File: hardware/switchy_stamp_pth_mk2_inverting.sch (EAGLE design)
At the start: 20 parts, among them IC1 MC34063

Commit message: fixed a few mistakes, still rearranging
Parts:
- C1: value 68uF -> 100uF
- H1, H2, H3, H4: value HOLE#4 -> HOLE#2; device A_butts:HOLE#4 -> A_butts:HOLE#2
- L1: device A_butts:INDUCTORRLB0912 -> A_butts:INDUCTORRADIAL-PTH-3-BY-6.7DIA
- ON/OFF: value SWITCH-SPDTPTH-RA-2.54MM -> SWITCH-SPDTPTH-VERT-2.54MM; device A_butts:SWITCH-SPDTPTH-RA-2.54MM -> A_butts:SWITCH-SPDTPTH-VERT-2.54MM
- R3: device A_butts:RESISTOR -> A_butts:RESISTORAXIAL-PTH-7.68MM
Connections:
- net N$6: now also L1.1
- net VOUT-: no longer L1.1
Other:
- moved on the sheet: C1, C2, C3, D1, D2, F1, IN, L1, LED1, ON/OFF, OUT, R4

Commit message: redo
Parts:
- R1, R2: device A_butts:RESISTORPTH-AXIAL-5.08MM -> A_butts:RESISTORAXIAL-PTH-7.68MM
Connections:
- net N$4: now also F1.1; no longer ON/OFF.COM
- net N$8: now also F1.2, ON/OFF.COM; no longer F1.1, ON/OFF.NC
- net VIN+: now also ON/OFF.NO; no longer F1.2
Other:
- moved on the sheet: F1, ON/OFF
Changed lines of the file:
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@@
 <?xml version="1.0" encoding="utf-8"?>
 <!DOCTYPE eagle SYSTEM "eagle.dtd">
-<eagle version="6.5.0">
+<eagle version="6.4">
 <drawing>
 <settings>
@@
 <setting verticaltext="up"/>
 </settings>
-<grid distance="100" unitdist="mil" unit="mil" style="lines" multiple="1" display="yes" altdistance="1" altunitdist="mil" altunit="mil"/>
+<grid distance="100" unitdist="mil" unit="mil" style="lines" multiple="1" display="yes" altdistance="1" altunitdist="mm" altunit="mm"/>
 <layers>
 <layer number="1" name="Top" color="4" fill="1" visible="yes" active="no"/>
@@
 <part name="F1" library="A_butts" deviceset="PTC" device="PTH"/>
 <part name="R3" library="A_butts" deviceset="RESISTOR" device="AXIAL-PTH-7.68MM" value="Iset"/>
-<part name="R1" library="A_butts" deviceset="RESISTOR" device="PTH-AXIAL-5.08MM" value="100R"/>
-<part name="R2" library="A_butts" deviceset="RESISTOR" device="PTH-AXIAL-5.08MM" value="300R"/>
+<part name="R1" library="A_butts" deviceset="RESISTOR" device="AXIAL-PTH-7.68MM" value="100R"/>
+<part name="R2" library="A_butts" deviceset="RESISTOR" device="AXIAL-PTH-7.68MM" value="300R"/>
 <part name="D2" library="A_butts" deviceset="DIODE-SCHOTTKY" device="DO-41" value="1N5819"/>
 <part name="D1" library="A_butts" deviceset="DIODE-SCHOTTKY" device="DO-41" value="1N5819"/>
@@
 <instance part="C2" gate="G$1" x="134.62" y="15.24"/>
 <instance part="C3" gate="G$1" x="104.14" y="33.02"/>
-<instance part="F1" gate="G$1" x="35.56" y="40.64" rot="R180"/>
+<instance part="F1" gate="G$1" x="48.26" y="25.4" rot="R180"/>
 <instance part="R3" gate="G$1" x="68.58" y="48.26"/>
 <instance part="R1" gate="G$1" x="73.66" y="15.24" rot="R90"/>
@@
 <instance part="H1" gate="G$1" x="119.38" y="66.04"/>
 <instance part="H3" gate="G$1" x="119.38" y="60.96"/>
-<instance part="ON/OFF" gate="G$1" x="40.64" y="20.32" rot="MR0"/>
+<instance part="ON/OFF" gate="G$1" x="35.56" y="43.18" rot="MR0"/>
 </instances>
 <busses>
@@
 <pinref part="IN" gate="G$1" pin="1"/>
 <wire x1="22.86" y1="40.64" x2="25.4" y2="40.64" width="0.1524" layer="91"/>
-<pinref part="F1" gate="G$1" pin="2"/>
-<wire x1="25.4" y1="40.64" x2="27.94" y2="40.64" width="0.1524" layer="91"/>
+<pinref part="ON/OFF" gate="G$1" pin="NO"/>
+<wire x1="25.4" y1="40.64" x2="30.48" y2="40.64" width="0.1524" layer="91"/>
 <junction x="25.4" y="40.64"/>
 </segment>
@@
 <net name="N$5" class="0">
 <segment>
-<pinref part="D1" gate="G$1" pin="C"/>
 <pinref part="R3" gate="G$1" pin="1"/>
 <wire x1="63.5" y1="48.26" x2="60.96" y2="48.26" width="0.1524" layer="91"/>
 <wire x1="60.96" y1="48.26" x2="60.96" y2="38.1" width="0.1524" layer="91"/>
-<wire x1="60.96" y1="38.1" x2="58.42" y2="38.1" width="0.1524" layer="91"/>
 <junction x="60.96" y="38.1"/>
 <pinref part="IC1" gate="G$1" pin="VCC"/>
@@
 <wire x1="60.96" y1="38.1" x2="60.96" y2="17.78" width="0.1524" layer="91"/>
 <junction x="60.96" y="38.1"/>
+<pinref part="D1" gate="G$1" pin="C"/>
+<wire x1="58.42" y1="38.1" x2="60.96" y2="38.1" width="0.1524" layer="91"/>
 </segment>
 </net>
@@
 </segment>
 </net>
-<net name="N$4" class="0">
-<segment>
-<pinref part="D1" gate="G$1" pin="A"/>
-<pinref part="ON/OFF" gate="G$1" pin="COM"/>
-<wire x1="45.72" y1="20.32" x2="50.8" y2="20.32" width="0.1524" layer="91"/>
-<wire x1="50.8" y1="20.32" x2="50.8" y2="38.1" width="0.1524" layer="91"/>
-<wire x1="50.8" y1="38.1" x2="53.34" y2="38.1" width="0.1524" layer="91"/>
-</segment>
-</net>
-<net name="N$8" class="0">
-<segment>
-<pinref part="F1" gate="G$1" pin="1"/>
-<pinref part="ON/OFF" gate="G$1" pin="NC"/>
-<wire x1="35.56" y1="22.86" x2="30.48" y2="22.86" width="0.1524" layer="91"/>
-<wire x1="30.48" y1="22.86" x2="30.48" y2="33.02" width="0.1524" layer="91"/>
-<wire x1="30.48" y1="33.02" x2="43.18" y2="33.02" width="0.1524" layer="91"/>
-<wire x1="43.18" y1="33.02" x2="43.18" y2="40.64" width="0.1524" layer="91"/>
-<wire x1="43.18" y1="40.64" x2="40.64" y2="40.64" width="0.1524" layer="91"/>
-</segment>
-</net>
 <net name="N$6" class="0">
 <segment>
@@
 </segment>
 </net>
+<net name="N$4" class="0">
+<segment>
+<pinref part="D1" gate="G$1" pin="A"/>
+<pinref part="F1" gate="G$1" pin="1"/>
+<wire x1="53.34" y1="25.4" x2="53.34" y2="38.1" width="0.1524" layer="91"/>
+</segment>
+</net>
+<net name="N$8" class="0">
+<segment>
+<pinref part="F1" gate="G$1" pin="2"/>
+<pinref part="ON/OFF" gate="G$1" pin="COM"/>
+<wire x1="40.64" y1="43.18" x2="40.64" y2="25.4" width="0.1524" layer="91"/>
+</segment>
+</net>

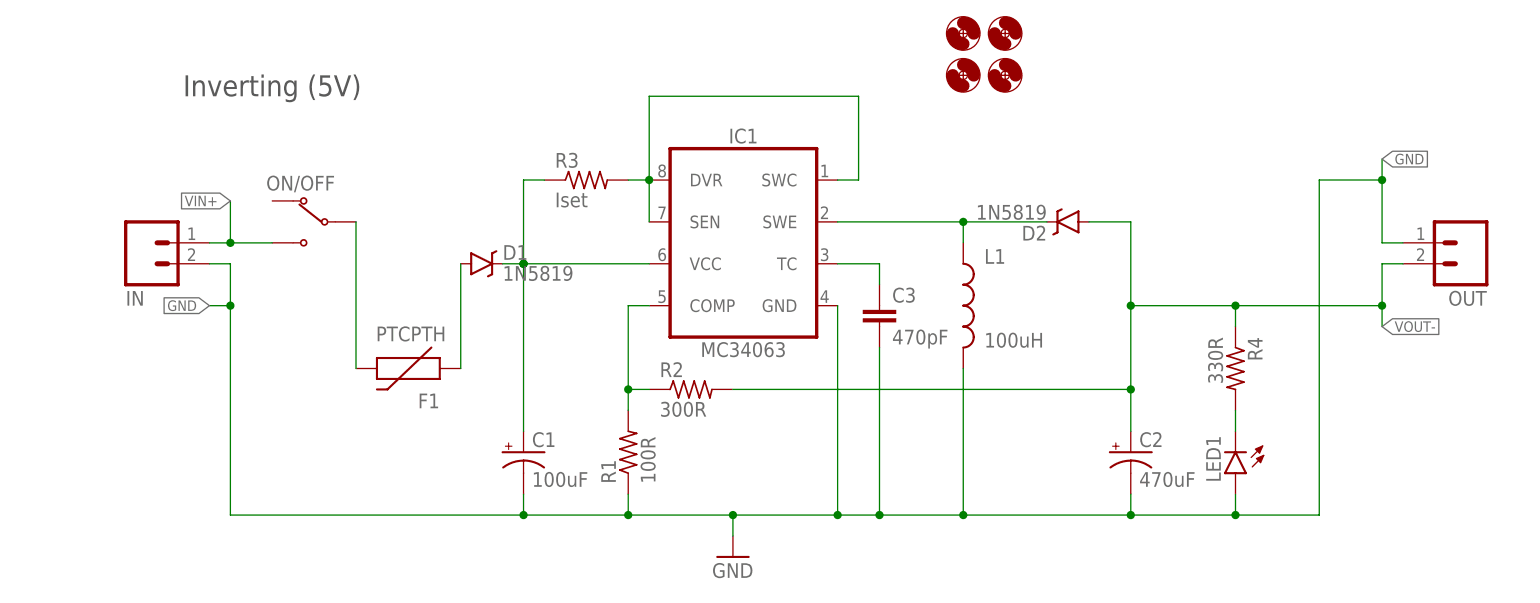
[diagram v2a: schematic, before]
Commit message: a saner layout with a few fixes, but still not complete
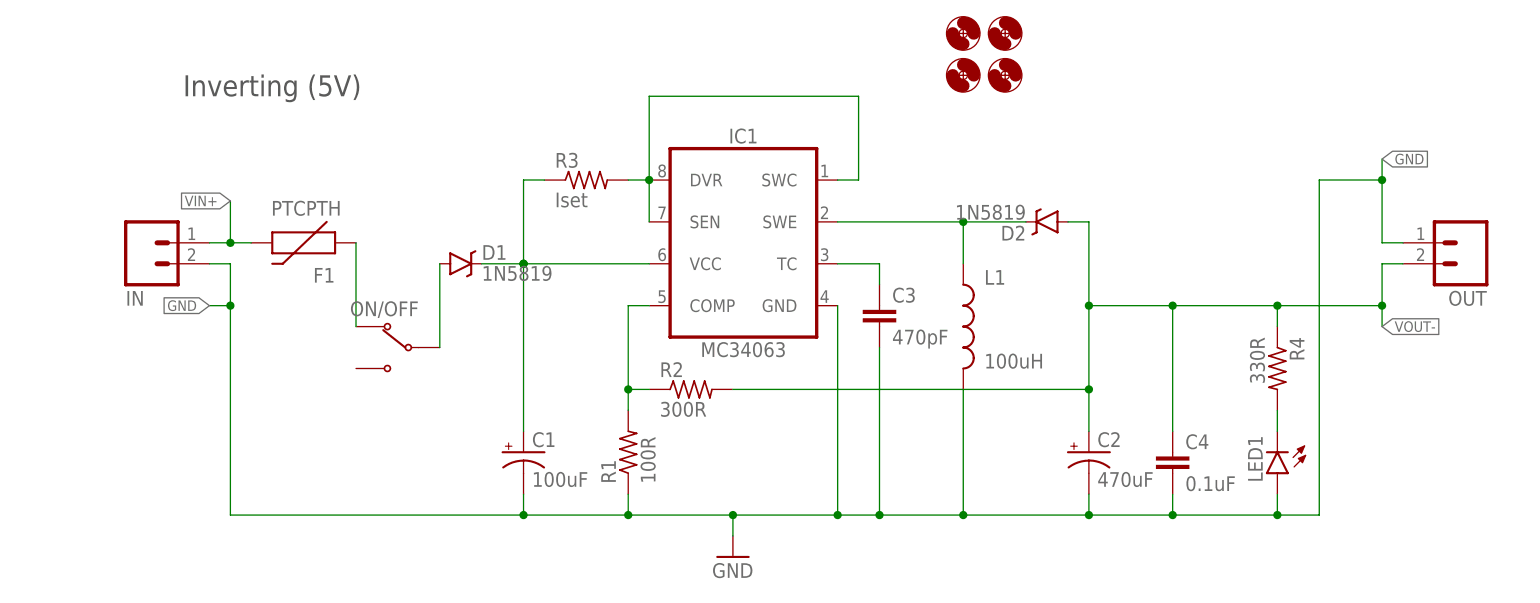
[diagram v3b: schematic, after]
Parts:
- added C4: 0.1uF, A_butts:CAPACITOR-CERAMIC025-024X044
- C1: device A_butts:CAPACITOR-POLARIZEDE2.5-6 -> A_butts:CAPACITOR-POLARIZEDE2.5-7
- ON/OFF: value SWITCH-SPDTPTH-VERT-2.54MM -> SWITCH-SPDTPTH-RA-2.54MM; device A_butts:SWITCH-SPDTPTH-VERT-2.54MM -> A_butts:SWITCH-SPDTPTH-RA-2.54MM
- R1, R2, R3: device A_butts:RESISTORAXIAL-PTH-7.68MM -> A_butts:RESISTORPTH-AXIAL-7.68MM
- R4: device A_butts:RESISTORPTH-AXIAL-5.08MM -> A_butts:RESISTORPTH-AXIAL-7.68MM
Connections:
- net GND: now also C4.2
- net N$4: now also ON/OFF.NC; no longer D1.A
- net N$8: now also D1.A; no longer F1.2
- net VIN+: now also F1.2; no longer ON/OFF.NO
- net VOUT-: now also C4.1
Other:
- moved on the sheet: C2, D1, D2, F1, L1, LED1, ON/OFF, R4

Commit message: blah
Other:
- moved on the sheet: L1
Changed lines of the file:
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@@
 <?xml version="1.0" encoding="utf-8"?>
 <!DOCTYPE eagle SYSTEM "eagle.dtd">
-<eagle version="6.5.0">
+<eagle version="6.4">
 <drawing>
 <settings>
@@
 <grid distance="100" unitdist="mil" unit="mil" style="lines" multiple="1" display="yes" altdistance="1" altunitdist="mil" altunit="mil"/>
 <layers>
-<layer number="1" name="Top" color="4" fill="1" visible="yes" active="no"/>
-<layer number="16" name="Bottom" color="1" fill="1" visible="yes" active="no"/>
-<layer number="17" name="Pads" color="2" fill="1" visible="yes" active="no"/>
-<layer number="18" name="Vias" color="2" fill="1" visible="yes" active="no"/>
-<layer number="19" name="Unrouted" color="6" fill="1" visible="yes" active="no"/>
-<layer number="20" name="Dimension" color="15" fill="1" visible="yes" active="no"/>
-<layer number="21" name="tPlace" color="7" fill="1" visible="yes" active="no"/>
-<layer number="22" name="bPlace" color="7" fill="1" visible="yes" active="no"/>
-<layer number="23" name="tOrigins" color="15" fill="1" visible="yes" active="no"/>
-<layer number="24" name="bOrigins" color="15" fill="1" visible="yes" active="no"/>
-<layer number="25" name="tNames" color="7" fill="1" visible="yes" active="no"/>
-<layer number="26" name="bNames" color="7" fill="1" visible="yes" active="no"/>
-<layer number="27" name="tValues" color="7" fill="1" visible="yes" active="no"/>
-<layer number="28" name="bValues" color="7" fill="1" visible="yes" active="no"/>
+<layer number="1" name="Top" color="4" fill="1" visible="no" active="no"/>
+<layer number="16" name="Bottom" color="1" fill="1" visible="no" active="no"/>
+<layer number="17" name="Pads" color="2" fill="1" visible="no" active="no"/>
+<layer number="18" name="Vias" color="2" fill="1" visible="no" active="no"/>
+<layer number="19" name="Unrouted" color="6" fill="1" visible="no" active="no"/>
+<layer number="20" name="Dimension" color="15" fill="1" visible="no" active="no"/>
+<layer number="21" name="tPlace" color="7" fill="1" visible="no" active="no"/>
+<layer number="22" name="bPlace" color="7" fill="1" visible="no" active="no"/>
+<layer number="23" name="tOrigins" color="15" fill="1" visible="no" active="no"/>
+<layer number="24" name="bOrigins" color="15" fill="1" visible="no" active="no"/>
+<layer number="25" name="tNames" color="7" fill="1" visible="no" active="no"/>
+<layer number="26" name="bNames" color="7" fill="1" visible="no" active="no"/>
+<layer number="27" name="tValues" color="7" fill="1" visible="no" active="no"/>
+<layer number="28" name="bValues" color="7" fill="1" visible="no" active="no"/>
 <layer number="29" name="tStop" color="7" fill="3" visible="no" active="no"/>
 <layer number="30" name="bStop" color="7" fill="6" visible="no" active="no"/>
@@
 <layer number="35" name="tGlue" color="7" fill="4" visible="no" active="no"/>
 <layer number="36" name="bGlue" color="7" fill="5" visible="no" active="no"/>
-<layer number="37" name="tTest" color="7" fill="1" visible="yes" active="no"/>
-<layer number="38" name="bTest" color="7" fill="1" visible="yes" active="no"/>
+<layer number="37" name="tTest" color="7" fill="1" visible="no" active="no"/>
+<layer number="38" name="bTest" color="7" fill="1" visible="no" active="no"/>
 <layer number="39" name="tKeepout" color="4" fill="11" visible="no" active="no"/>
 <layer number="40" name="bKeepout" color="1" fill="11" visible="no" active="no"/>
@@
 <layer number="44" name="Drills" color="7" fill="1" visible="no" active="no"/>
 <layer number="45" name="Holes" color="7" fill="1" visible="no" active="no"/>
-<layer number="46" name="Milling" color="3" fill="1" visible="yes" active="no"/>
-<layer number="47" name="Measures" color="7" fill="1" visible="yes" active="no"/>
-<layer number="48" name="Document" color="7" fill="1" visible="yes" active="no"/>
-<layer number="49" name="Reference" color="7" fill="1" visible="yes" active="no"/>
-<layer number="50" name="dxf" color="7" fill="1" visible="yes" active="no"/>
-<layer number="51" name="tDocu" color="7" fill="1" visible="yes" active="no"/>
-<layer number="52" name="bDocu" color="7" fill="1" visible="yes" active="no"/>
-<layer number="53" name="tGND_GNDA" color="7" fill="9" visible="yes" active="no"/>
-<layer number="54" name="bGND_GNDA" color="1" fill="9" visible="yes" active="no"/>
-<layer number="56" name="wert" color="7" fill="1" visible="yes" active="no"/>
-<layer number="57" name="tCAD" color="7" fill="1" visible="yes" active="no"/>
+<layer number="46" name="Milling" color="3" fill="1" visible="no" active="no"/>
+<layer number="47" name="Measures" color="7" fill="1" visible="no" active="no"/>
+<layer number="48" name="Document" color="7" fill="1" visible="no" active="no"/>
+<layer number="49" name="Reference" color="7" fill="1" visible="no" active="no"/>
+<layer number="50" name="dxf" color="7" fill="1" visible="no" active="no"/>
+<layer number="51" name="tDocu" color="7" fill="1" visible="no" active="no"/>
+<layer number="52" name="bDocu" color="7" fill="1" visible="no" active="no"/>
+<layer number="53" name="tGND_GNDA" color="7" fill="9" visible="no" active="no"/>
+<layer number="54" name="bGND_GNDA" color="1" fill="9" visible="no" active="no"/>
+<layer number="56" name="wert" color="7" fill="1" visible="no" active="no"/>
+<layer number="57" name="tCAD" color="7" fill="1" visible="no" active="no"/>
 <layer number="91" name="Nets" color="2" fill="1" visible="yes" active="yes"/>
 <layer number="92" name="Busses" color="1" fill="1" visible="yes" active="yes"/>
@@
 </plain>
 <instances>
-<instance part="L1" gate="G$1" x="114.3" y="30.48"/>
+<instance part="L1" gate="G$1" x="114.3" y="33.02"/>
 <instance part="C1" gate="G$1" x="60.96" y="15.24"/>
 <instance part="C2" gate="G$1" x="129.54" y="15.24"/>
@@
 <junction x="99.06" y="7.62"/>
 <pinref part="L1" gate="G$1" pin="2"/>
-<wire x1="114.3" y1="7.62" x2="114.3" y2="22.86" width="0.1524" layer="91"/>
+<wire x1="114.3" y1="7.62" x2="114.3" y2="25.4" width="0.1524" layer="91"/>
 <wire x1="104.14" y1="7.62" x2="114.3" y2="7.62" width="0.1524" layer="91"/>
 <junction x="104.14" y="7.62"/>
@@
 <segment>
 <pinref part="L1" gate="G$1" pin="1"/>
-<wire x1="114.3" y1="43.18" x2="114.3" y2="38.1" width="0.1524" layer="91"/>
+<wire x1="114.3" y1="43.18" x2="114.3" y2="40.64" width="0.1524" layer="91"/>
 <pinref part="IC1" gate="G$1" pin="SWE"/>
 <wire x1="99.06" y1="43.18" x2="114.3" y2="43.18" width="0.1524" layer="91"/>
